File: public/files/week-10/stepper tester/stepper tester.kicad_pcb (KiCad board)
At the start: 2 copper layers, 102.5 x 39.5 mm, 29 parts, among them J1 PROG, J2 2.54mm_Vertical_THT, J3 Screw_Terminal_01x02_P3.5mm, J9 S4B-PH-SM4-TB, SW1 SMD_6x3.5mm_h2.5mm, SW2 NDS-03V_C501525, U1 AMS1117-3.3, U2 ESP32-WROOM-32E, U3 DRV8825_STEPPER_MOTOR_DRIVER_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

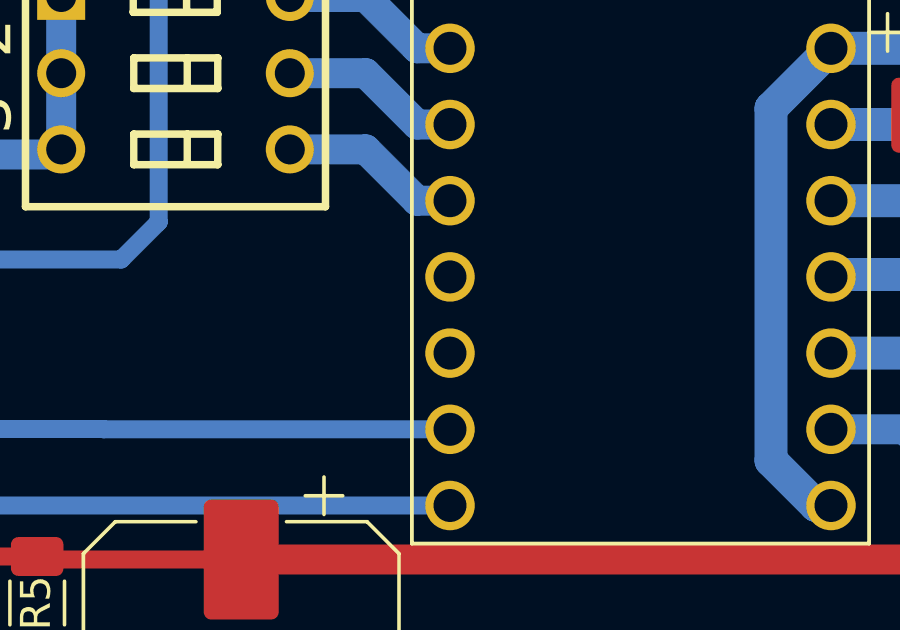
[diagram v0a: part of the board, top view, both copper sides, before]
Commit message: 3d scanning sections added
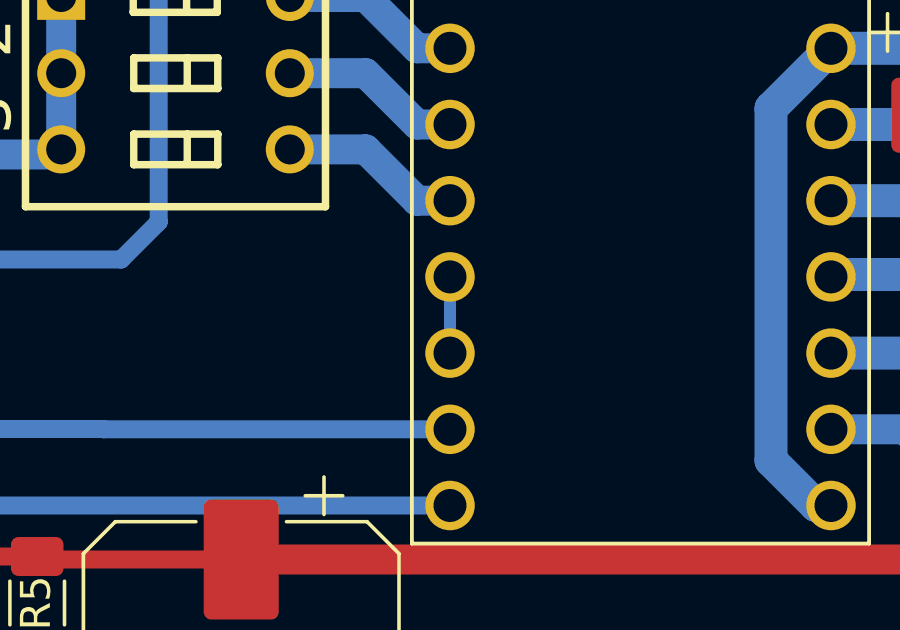
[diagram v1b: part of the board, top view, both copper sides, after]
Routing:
- net Net-(U3-~{RST}): track 0.00 -> 2.54 mm
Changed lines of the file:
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@@
+	)
+	(segment
+		(start 89.96 57.33)
+		(end 89.96 59.87)
+		(width 0.4)
+		(layer "B.Cu")
+		(net 39)
 	)
 	(segment
